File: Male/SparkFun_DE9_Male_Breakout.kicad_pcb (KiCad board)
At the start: 4 copper layers, 22.9 x 31.5 mm, 43 parts, among them J1 Conn_01x01, J2 Conn_01x09, J3 DE9-Male, J4 Conn_01x01

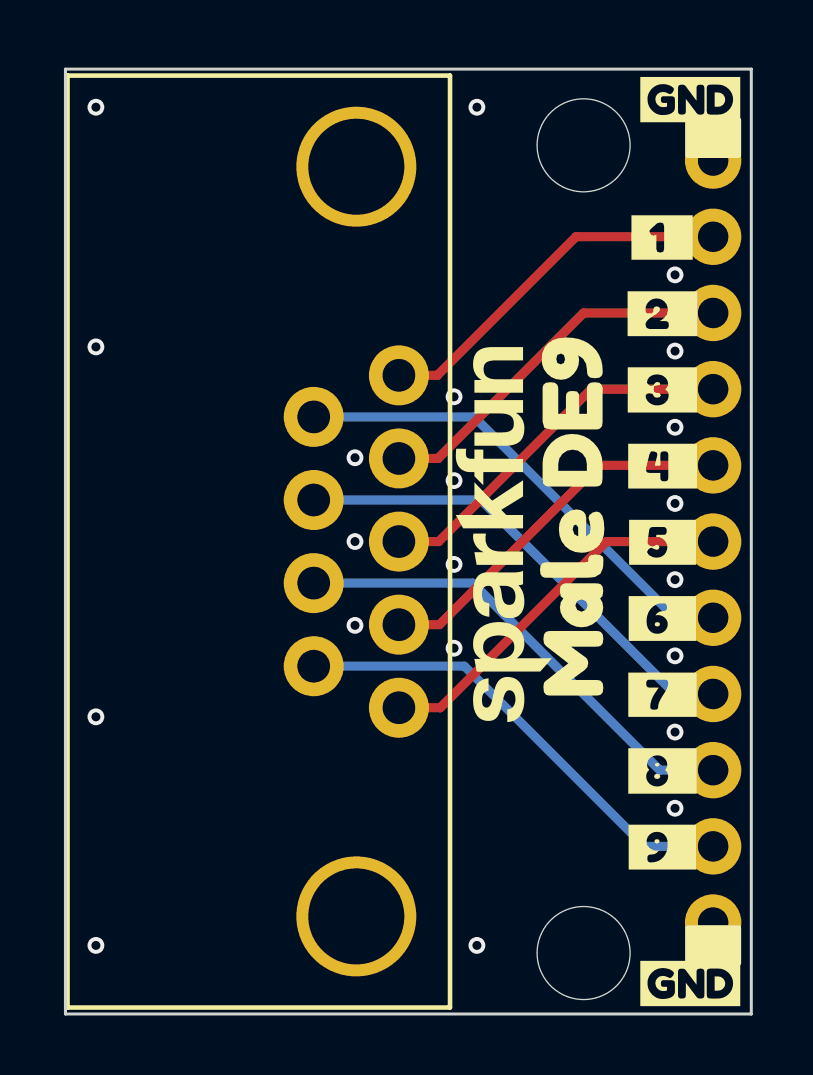
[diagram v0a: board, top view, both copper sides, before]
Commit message: Updates DE9 layout by placing components more consistently on grid
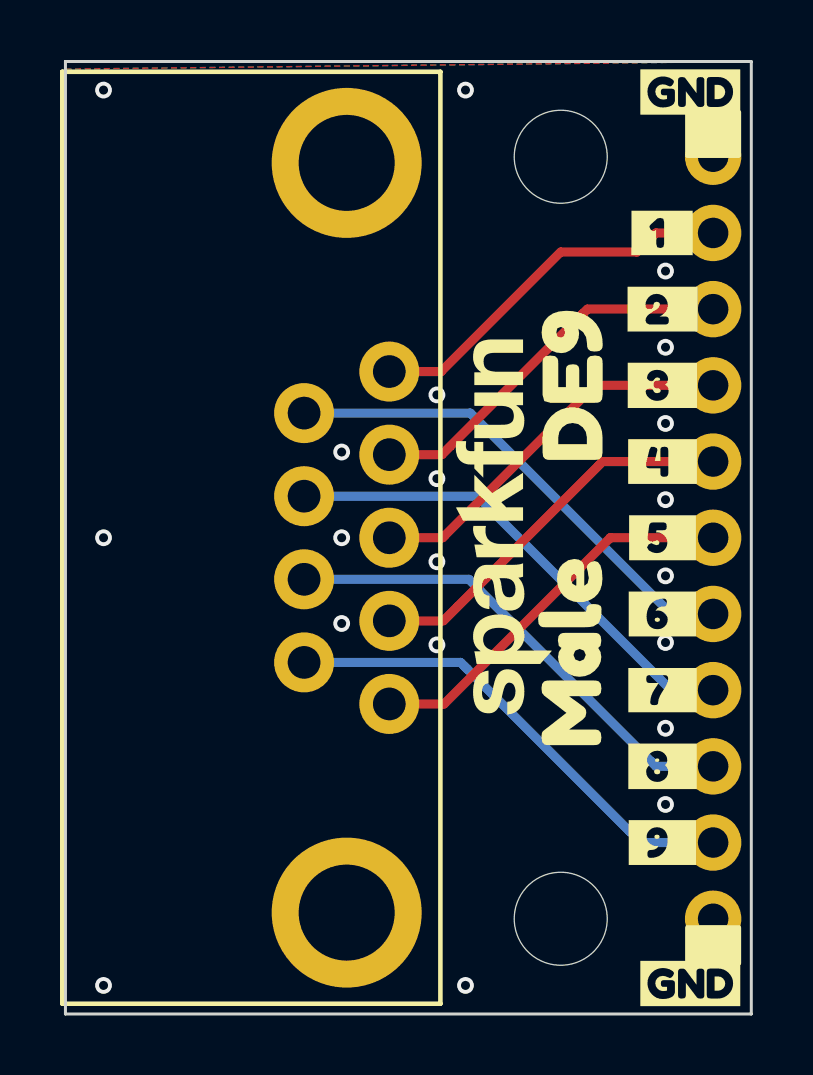
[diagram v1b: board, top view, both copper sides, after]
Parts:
- removed J3: DE9-Male, DE9-Footprint:DB9
- added J5: DE9-Male, DE9-Footprint:DE9, F.Cu at (126.4, 108.6)
- moved kibuzzard-67DB37C8 1.65 mm to (132.4, 112.4)
- moved ST2 1.37 mm to (132.1, 121.3)
- moved kibuzzard-67D49838 0.89 mm to (132.5, 103.5)
- moved ST1 0.85 mm to (132.1, 95.9)
- moved G*** 0.35 mm to (119.4, 96.8)
- moved kibuzzard-67DDBC91 0.30 mm to (136.4, 93.7)
- moved G*** 0.25 mm to (129.9, 108.6)
- moved kibuzzard-67DDBC91 0.25 mm to (136.4, 93.7)
- moved kibuzzard-67D49687 0.15 mm to (135.5, 98.4)
- moved kibuzzard-67D496B8 0.15 mm to (135.5, 101.0)
- moved kibuzzard-67D496C7 0.15 mm to (135.5, 103.5)
- moved kibuzzard-67D496CD 0.15 mm to (135.5, 106.0)
- moved kibuzzard-67D496D5 0.15 mm to (135.5, 108.6)
- moved kibuzzard-67D496DD 0.15 mm to (135.5, 111.1)
- moved kibuzzard-67D496E4 0.15 mm to (135.5, 113.7)
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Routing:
- net /2: track 12.5 -> 13.0 mm
- net GND: vias 21 -> 20
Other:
- board size 22.9 x 31.5 mm -> 22.9 x 31.8 mm
- copper layers 4 -> 2

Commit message: Updates male breakout with new footprint
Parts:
- removed kibuzzard-67DDA384: G***, kibuzzard-67DDA384
- added kibuzzard-67F7FDBF: G***, kibuzzard-67F7FDBF, B.Cu at (135.6, 118.7)
- moved kibuzzard-67D49687 20.3 mm to (135.6, 118.7)
- moved kibuzzard-67D496F6 20.3 mm to (135.6, 98.4)
- moved kibuzzard-67DDA3E0 20.3 mm to (135.6, 98.4)
- moved J2 20.3 mm to (137.2, 118.7), turned to 90 degrees
- moved kibuzzard-67DDA391 15.2 mm to (135.6, 116.2)
- moved kibuzzard-67D496B8 15.2 mm to (135.6, 116.2)
- moved kibuzzard-67D496EA 15.2 mm to (135.6, 101.0)
- moved kibuzzard-67DDA3D5 15.2 mm to (135.6, 101.0)
- moved kibuzzard-67DDBDD7 11.1 mm to (128.5, 103.2)
- moved kibuzzard-67DDBDCA 10.9 mm to (128.6, 114.0)
- moved kibuzzard-67D496C7 10.2 mm to (135.6, 113.7)
- moved kibuzzard-67D496E4 10.2 mm to (135.6, 103.5)
- moved kibuzzard-67DDA399 10.2 mm to (135.6, 113.7)
- moved kibuzzard-67DDA3B8 10.2 mm to (135.6, 103.5)
- moved kibuzzard-67DDBDDC 8.58 mm to (121.5, 104.5)
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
